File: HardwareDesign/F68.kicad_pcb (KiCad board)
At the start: 2 copper layers, 150 x 90 mm, 46 parts, among them J001 Conn_02x40_Odd_Even, J701 RCJ-044, J702 Conn_01x02, J801 Conn_01x02, J802 Conn_02x09_Odd_Even, J803 SJ1-3525N, Q701 2N4401, U701 TMS9918A, U702 74HCT04, U703 74HCT32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

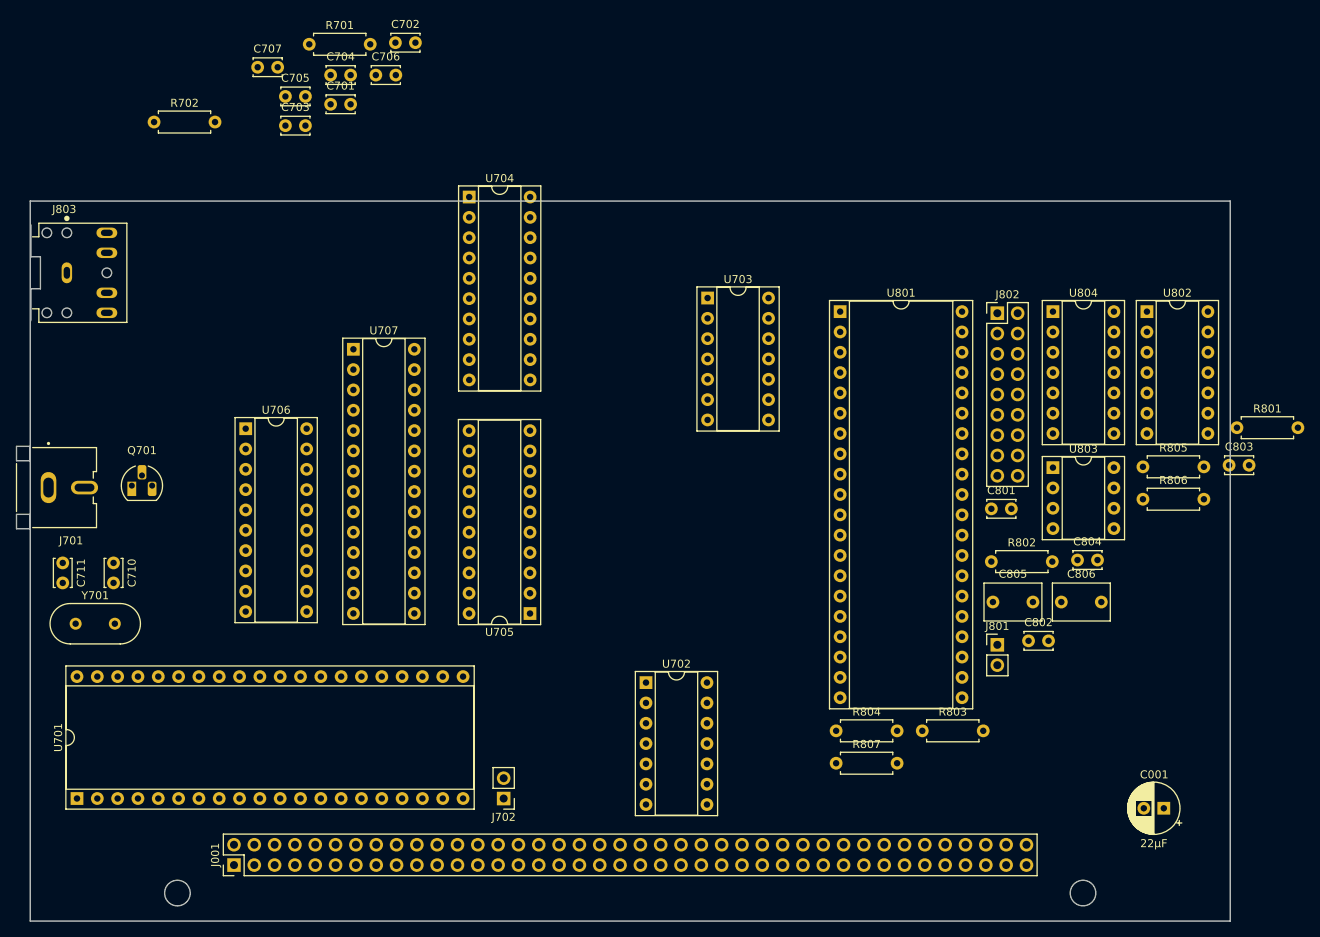
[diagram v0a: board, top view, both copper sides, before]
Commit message: move TMS9918A/YM2149F PCB to separate file
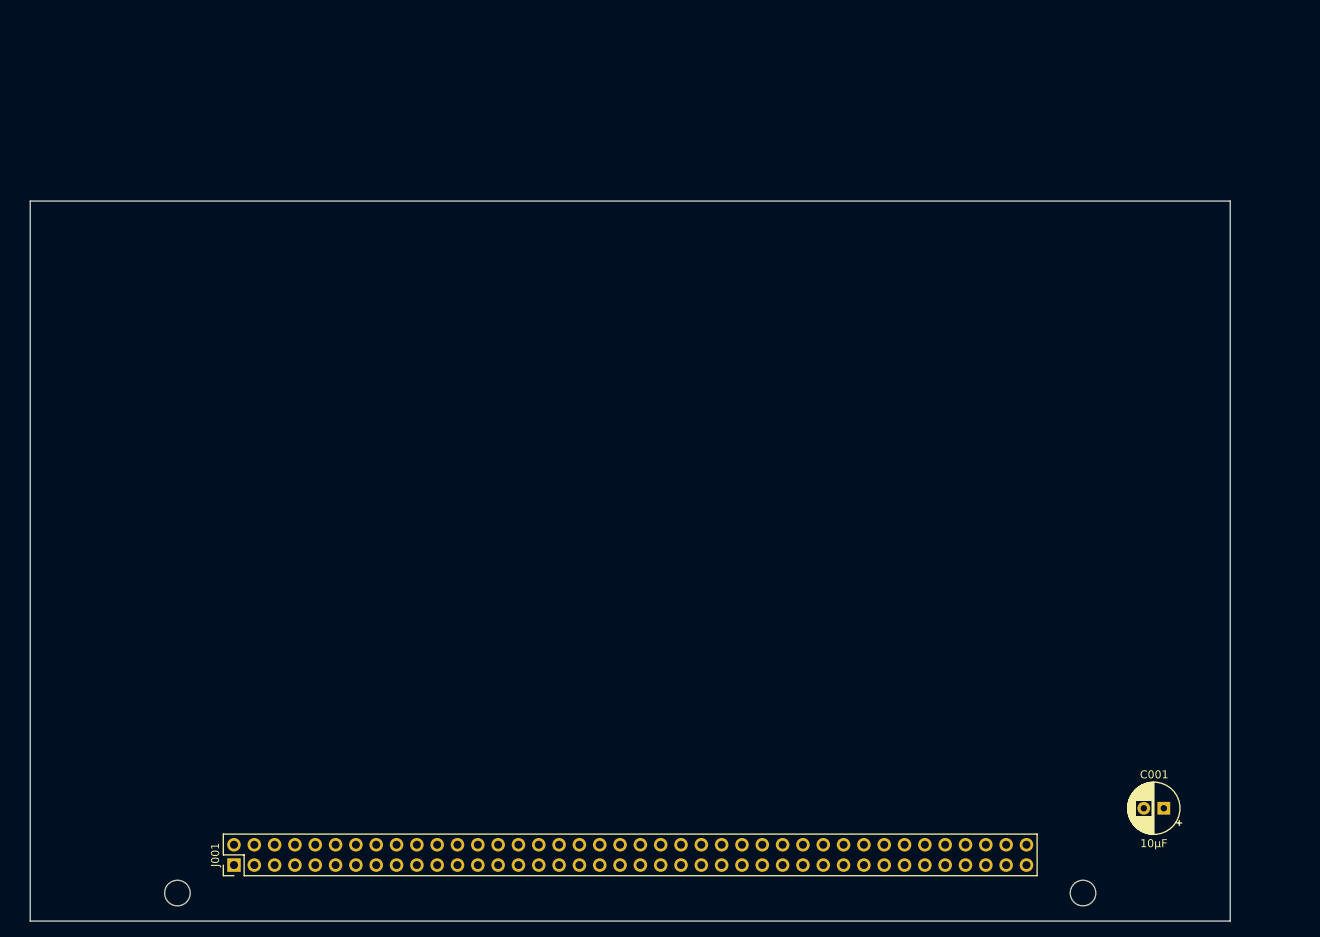
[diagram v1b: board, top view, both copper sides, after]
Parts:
- removed C701, C702, C703, C704, C705, C706, C707, C801, C802, C803, C804: 100 nF, Capacitor_THT:C_Disc_D3.4mm_W2.1mm_P2.50mm
- removed C710, C711: 22 pF, Capacitor_THT:C_Disc_D3.4mm_W2.1mm_P2.50mm
- removed C805, C806: 2.2 uF, Capacitor_THT:C_Rect_L7.0mm_W4.5mm_P5.00mm
- removed J701: RCJ-044, CUI_RCJ-044:CUI_RCJ-044
- removed J702, J801: Conn_01x02, Connector_PinHeader_2.54mm:PinHeader_1x02_P2.54mm_Vertical
- removed J802: Conn_02x09_Odd_Even, Connector_PinHeader_2.54mm:PinHeader_2x09_P2.54mm_Vertical
- removed J803: SJ1-3525N, CUI_SJ1-3525N:CUI_SJ1-3525N
- removed Q701: 2N4401, Package_TO_SOT_THT:TO-92_HandSolder
- removed R701: 470, Resistor_THT:R_Axial_DIN0207_L6.3mm_D2.5mm_P7.62mm_Horizontal
- removed R702, R804, R805, R806, R807: 1k, Resistor_THT:R_Axial_DIN0207_L6.3mm_D2.5mm_P7.62mm_Horizontal
- removed R801, R802, R803: 3k, Resistor_THT:R_Axial_DIN0207_L6.3mm_D2.5mm_P7.62mm_Horizontal
- removed U701: TMS9918A, Package_DIP:DIP-40_W15.24mm_Socket
- removed U702: 74HCT04, Package_DIP:DIP-14_W7.62mm_Socket
- removed U703: 74HCT32, Package_DIP:DIP-14_W7.62mm_Socket
- removed U704, U705, U706: 74HCT574, Package_DIP:DIP-20_W7.62mm_Socket
- removed U707: HM62256BLP-7, Package_DIP:DIP-28_W7.62mm_Socket
- removed U801: YM2149, Package_DIP:DIP-40_W15.24mm_Socket
- removed U802: 74HCT11, Package_DIP:DIP-14_W7.62mm_Socket
- removed U803: 4 MHz Osc (half can), Package_DIP:DIP-8_W7.62mm_Socket
- removed U804: 74HCT00, Package_DIP:DIP-14_W7.62mm_Socket
- removed Y701: 10.738635 MHz, Crystal:Crystal_HC18-U_Vertical
- C001: value 22μF -> 10μF
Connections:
- net /~{RAMEN} renamed Net-(J001-Pad64)
- J001 pad 1: unconnected-(J001-Pad1) -> Net-(J001-Pad1)
- J001 pad 2: unconnected-(J001-Pad2) -> Net-(J001-Pad2)
- J001 pad 37: unconnected-(J001-Pad37) -> Net-(J001-Pad37)
- J001 pad 39: unconnected-(J001-Pad39) -> Net-(J001-Pad39)
- J001 pad 52: unconnected-(J001-Pad52) -> Net-(J001-Pad52)
- J001 pad 54: unconnected-(J001-Pad54) -> Net-(J001-Pad54)
- J001 pad 56: unconnected-(J001-Pad56) -> Net-(J001-Pad56)
- J001 pad 58: unconnected-(J001-Pad58) -> Net-(J001-Pad58)
- J001 pad 60: unconnected-(J001-Pad60) -> Net-(J001-Pad60)
- J001 pad 62: unconnected-(J001-Pad62) -> Net-(J001-Pad62)
